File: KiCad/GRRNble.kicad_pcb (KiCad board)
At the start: 2 copper layers, 28 x 41 mm, 49 parts, among them J1 JST_SH_06, Q1 DMG3415U, Q2 BSS138, Q3 DMG3415U, SW1 SW_Push, SW2 SW_Push, SW3 SW_Push, U1 R5F100LJAFB, U2 BUZZER, U3 SSD1306, U4 MCP73831, U5 RN4020, U6 NJM2865F33, Y1 32.768k

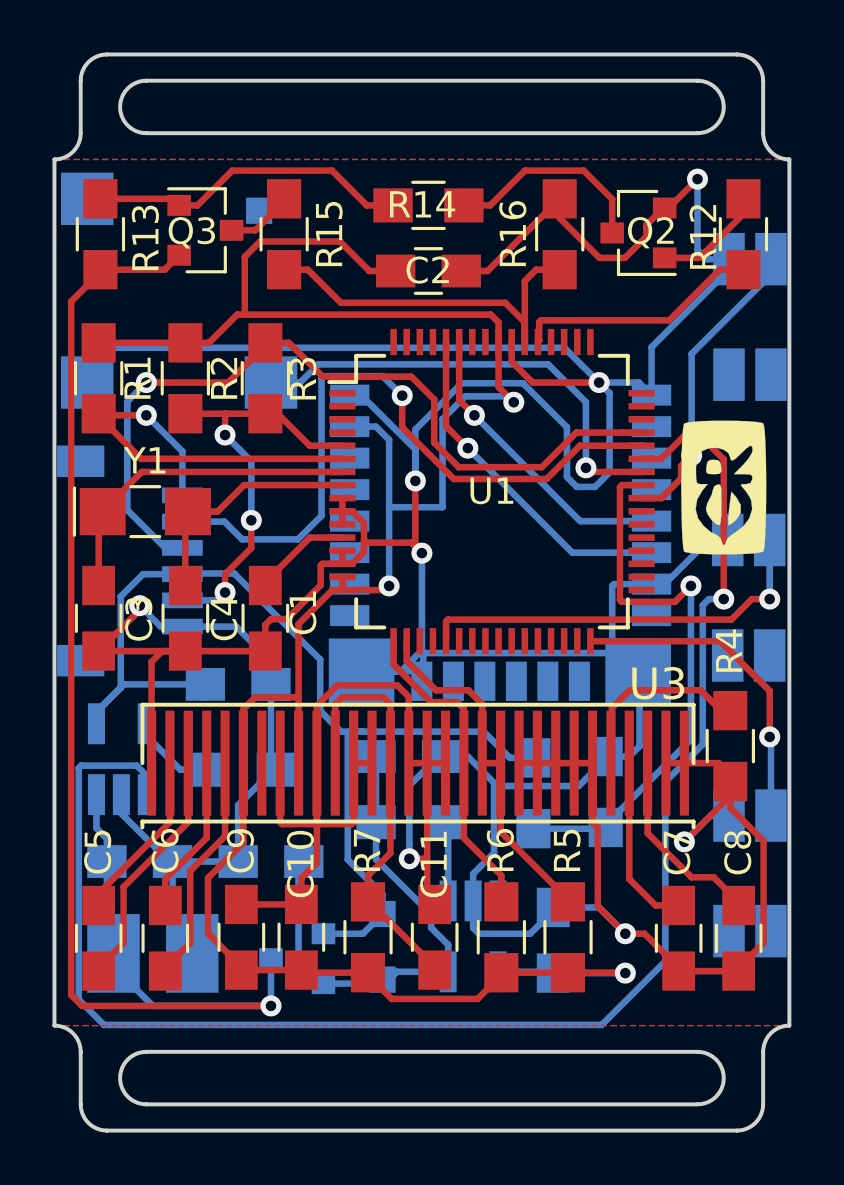
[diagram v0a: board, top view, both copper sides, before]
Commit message: change schematic layout
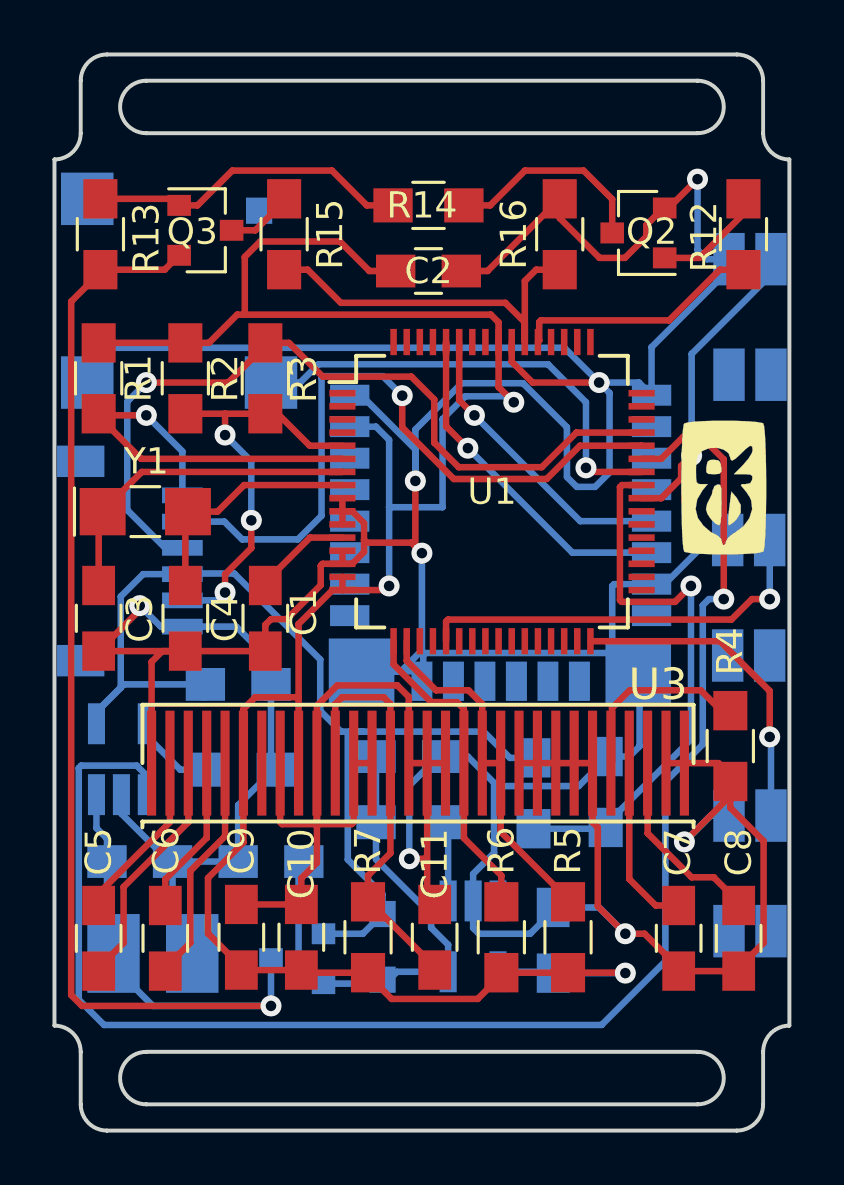
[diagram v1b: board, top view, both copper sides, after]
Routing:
- removed copper zone on B.Cu, net GND
- removed copper zone on F.Cu, net GND

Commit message: change PCB status
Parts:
- moved G*** 3.44 mm to (120.8, 92.7)
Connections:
- J1 pad M1: (no net) -> Net-(J1-PadM1)
- J1 pad M2: (no net) -> Net-(J1-PadM2)
- U1 pad 1: (no net) -> Net-(U1-Pad1)
- U1 pad 19: (no net) -> Net-(U1-Pad19)
- U1 pad 2: (no net) -> Net-(U1-Pad2)
- U1 pad 20: (no net) -> Net-(U1-Pad20)
- U1 pad 21: SW3 -> STAT
- U1 pad 22: (no net) -> Net-(U1-Pad22)
- U1 pad 23: (no net) -> Net-(U1-Pad23)
- U1 pad 24: (no net) -> Net-(U1-Pad24)
- U1 pad 25: (no net) -> Net-(U1-Pad25)
- U1 pad 26: (no net) -> Net-(U1-Pad26)
- U1 pad 27: (no net) -> Net-(U1-Pad27)
- U1 pad 28: (no net) -> Net-(U1-Pad28)
- U1 pad 29: (no net) -> VDD
- U1 pad 3: (no net) -> Net-(U1-Pad3)
- U1 pad 30: (no net) -> Net-(U1-Pad30)
- U1 pad 31: (no net) -> Net-(U1-Pad31)
- U1 pad 32: SW1 -> Net-(U1-Pad32)
- U1 pad 33: (no net) -> Net-(U1-Pad33)
- U1 pad 34: (no net) -> Net-(U1-Pad34)
- U1 pad 35: (no net) -> Net-(U1-Pad35)
- U1 pad 36: (no net) -> Net-(U1-Pad36)
- U1 pad 37: (no net) -> Net-(U1-Pad37)
- U1 pad 38: (no net) -> Net-(U1-Pad38)
- U1 pad 39: (no net) -> Net-(U1-Pad39)
- U1 pad 4: (no net) -> Net-(U1-Pad4)
- U1 pad 40: SW2 -> SW3
- U1 pad 41: VDD -> SW1
- U1 pad 43: STAT -> SW2
- U1 pad 46: (no net) -> Net-(U1-Pad46)
- U1 pad 47: (no net) -> Net-(U1-Pad47)
- U1 pad 48: (no net) -> Net-(U1-Pad48)
- U1 pad 49: (no net) -> Net-(U1-Pad49)
- U1 pad 50: (no net) -> Net-(U1-Pad50)
- U1 pad 51: (no net) -> Net-(U1-Pad51)
- U1 pad 52: (no net) -> Net-(U1-Pad52)
- U1 pad 57: (no net) -> Net-(U1-Pad57)
- U1 pad 58: (no net) -> Net-(U1-Pad58)
- U1 pad 61: (no net) -> Net-(U1-Pad61)
- U1 pad 62: (no net) -> Net-(U1-Pad62)
- U1 pad 63: (no net) -> Net-(U1-Pad63)
- U1 pad 64: (no net) -> Net-(U1-Pad64)
- U2 pad 3: (no net) -> Net-(U2-Pad3)
- U2 pad 4: (no net) -> Net-(U2-Pad4)
- U3 pad 7: (no net) -> Net-(U3-Pad7)
- U5 pad 10: (no net) -> Net-(U5-Pad10)
- U5 pad 11: (no net) -> Net-(U5-Pad11)
- U5 pad 12: (no net) -> Net-(U5-Pad12)
- U5 pad 13: (no net) -> Net-(U5-Pad13)
- U5 pad 14: (no net) -> Net-(U5-Pad14)
- U5 pad 17: (no net) -> Net-(U5-Pad17)
- U5 pad 18: (no net) -> Net-(U5-Pad18)
- U5 pad 19: (no net) -> Net-(U5-Pad19)
- U5 pad 2: (no net) -> Net-(U5-Pad2)
- U5 pad 20: (no net) -> Net-(U5-Pad20)
- U5 pad 21: (no net) -> Net-(U5-Pad21)
- U5 pad 22: (no net) -> Net-(U5-Pad22)
- U5 pad 3: (no net) -> Net-(U5-Pad3)
- U5 pad 4: (no net) -> Net-(U5-Pad4)
- U5 pad 8: (no net) -> Net-(U5-Pad8)
- U6 pad 3: (no net) -> Net-(U6-Pad3)
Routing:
- net SW3: track 15.7 -> 6.19 mm
- net SW1: track 12.4 -> 17.8 mm
- net STAT: track 60.3 -> 63.9 mm
- net VDD: track 21.5 -> 19.9 mm
- net GND: track 252.9 -> 251.8 mm
- net Net-(C7-Pad1): track 6.72 -> 6.20 mm

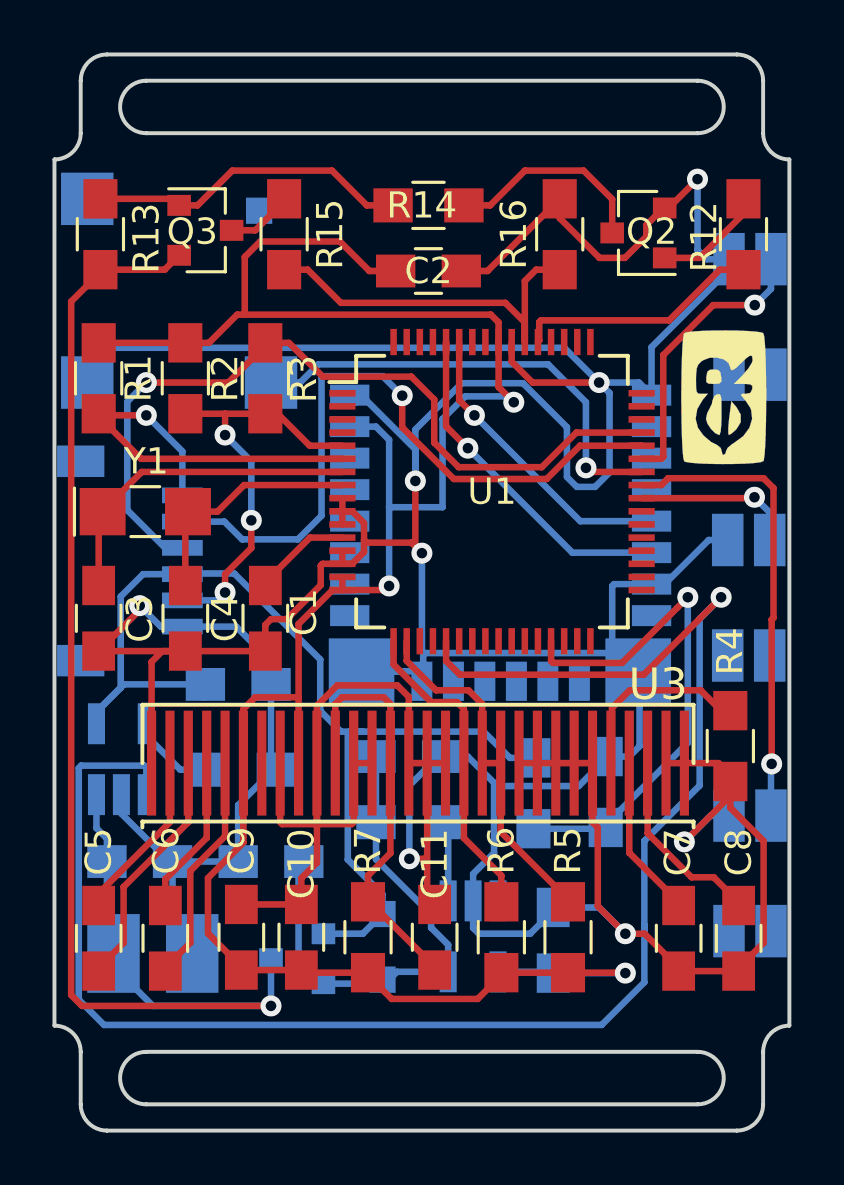
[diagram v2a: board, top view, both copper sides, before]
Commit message: change PCB layout
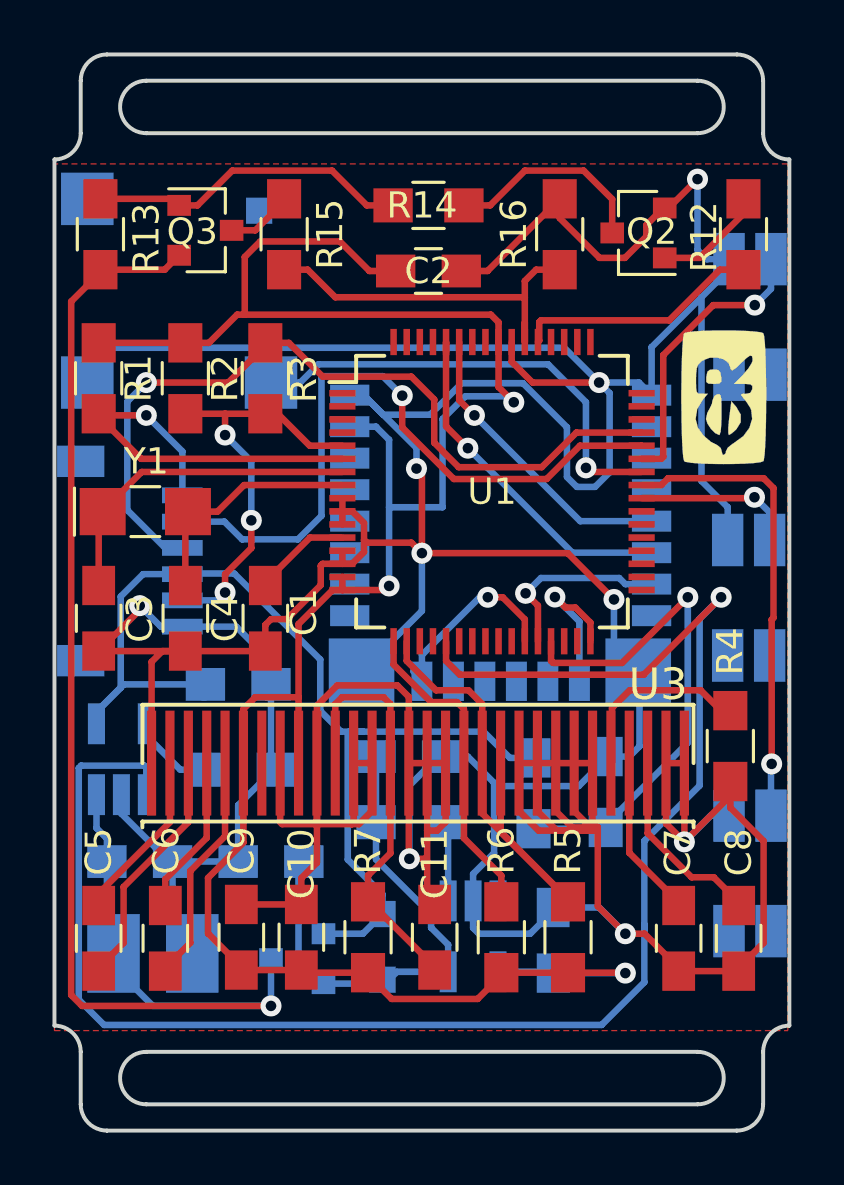
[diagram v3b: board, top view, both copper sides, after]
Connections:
- U1 pad 27: Net-(U1-Pad27) -> WAKEHW
- U1 pad 28: Net-(U1-Pad28) -> WAKESW
- U1 pad 32: Net-(U1-Pad32) -> PIO1
- U5 pad 10: Net-(U5-Pad10) -> PIO1
- U5 pad 15: GND -> WAKEHW
- U5 pad 7: GND -> WAKESW
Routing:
- net GND: track 251.8 -> 282.2 mm, vias 8 -> 9
- net SDA: track 13.6 -> 21.3 mm
- net WAKESW: track 0.00 -> 7.65 mm, vias 0 -> 1
- net WAKEHW: track 0.00 -> 7.55 mm, vias 0 -> 1
- net PIO1: track 0.00 -> 6.06 mm, vias 0 -> 1
- added copper zone on F.Cu, net GND

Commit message: update gerber files
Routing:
- added copper zone on B.Cu, net GND
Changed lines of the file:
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@@
     (visible_elements 7FFDFF69)
     (pcbplotparams
-      (layerselection 0x010f0_80000001)
+      (layerselection 0x010f0_ffffffff)
       (usegerberextensions true)
       (usegerberattributes false)
@@
       )
     )
+  )
+  (zone (net 1) (net_name GND) (layer B.Cu) (hatch edge 0.508)
+    (connect_pads (clearance 0.508))
+    (min_thickness 0.254)
+    (fill yes (arc_segments 16) (thermal_gap 0.508) (thermal_bridge_width 0.508))
+    (polygon
+      (pts
+        (xy 95.25 83.82) (xy 123.19 83.82) (xy 123.19 116.84) (xy 95.25 116.84)
+      )
+    )

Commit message: WIP:Change schematic
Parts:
- removed C14: 1.0uF, Capacitors_SMD:C_0805_HandSoldering
- C15: value 0.1uF -> 1.0uF
- G***: moved to B.Cu
- R11: footprint Resistors_SMD:R_0805_HandSoldering -> Resistor_SMD:R_0805_2012Metric_Pad1.15x1.40mm_HandSolder
- U6: value NJM2865F33 -> MCP1703A-3302_SOT23; footprint TO_SOT_Packages_SMD:SOT-23-5_HandSoldering -> Package_TO_SOT_SMD:SOT-23
- moved G*** 24.2 mm to (103.8, 109.9), turned to 180 degrees
- moved C15 2.80 mm to (109.2, 109.2), turned to 180 degrees
- moved R11 2.78 mm to (109.2, 106.2), turned to 180 degrees
- moved U6 0.68 mm to (111.0, 113.9), turned to 180 degrees
- moved R8 0.25 mm to (102.3, 106.7)
- moved U2 0.25 mm to (100.0, 88.9), turned to 90 degrees
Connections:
- R11 pad 1: +5V -> Net-(C12-Pad1)
- R11 pad 2: Net-(R11-Pad2) -> GND
- U1 pad 42: Net-(U1-Pad42) -> SW2
- U1 pad 43: SW2 -> Net-(U1-Pad43)
- U2 pad 1: Net-(U1-Pad42) -> Net-(U1-Pad43)
- U6 pad 1: Net-(R11-Pad2) -> GND
- U6 pad 2: GND -> +3V3
- U6 pad 3: Net-(U6-Pad3) -> +5V
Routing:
- net Net-(U1-Pad43): track 0.00 -> 29.9 mm, vias 0 -> 1
- net Net-(U1-Pad42): track 17.6 -> 0.00 mm, vias 1 -> 0
- net +5V: track 19.3 -> 10.6 mm
- net GND: track 282.2 -> 278.5 mm, vias 9 -> 8
- net Net-(R11-Pad2): track 3.02 -> 0.00 mm
- net SW1: track 17.8 -> 15.2 mm
- net Net-(C12-Pad1): track 40.7 -> 43.2 mm
- net SW3: track 6.19 -> 8.55 mm
- net +3V3: track 87.5 -> 88.8 mm
- net RXD: track 26.3 -> 25.2 mm
- net TXD: track 30.9 -> 30.2 mm
- net WAKEHW: track 7.55 -> 7.01 mm
- removed copper zone on B.Cu, net GND
- removed copper zone on F.Cu, net GND
